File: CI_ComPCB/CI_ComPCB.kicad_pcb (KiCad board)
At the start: 2 copper layers, 145 x 101 mm, 30 parts, among them J1 Conn_01x15_Female, J10 Conn_01x02_Male, J1001 Conn_01x06_Female, J1002 Conn_01x06_Female, J1003 Conn_02x04_Odd_Even, J11 Conn_01x02_Male, J12 Conn_01x01_Female, J13 Conn_01x01_Female, J2 Conn_01x02_Male, J4 Conn_01x15_Female, J6 Conn_01x02_Male, J7 Conn_01x03_Male, J8 RJ45_LED_Shielded, J9 RJ45_LED_Shielded, Q1 IRF9540N, Q2 IRF9540N, U1 Boost_Converter, U1001 ESP32s

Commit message: Rough V1
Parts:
- removed Buck_Converter1: 12v_to_5V, RackCom:12vto5v
- removed Converter1, Converter2: TxRx-RS485, RackCom:TXRX-AB
- removed D1, D2, D3: 1N5400, Diode_THT:D_DO-201AD_P15.24mm_Horizontal
- removed HW-3731: Charger, RackCom:Charger
- removed Holder1: Battery-New_Library, RackCom:Battery
- removed J1, J4: Conn_01x15_Female, Connector_PinSocket_2.54mm:PinSocket_1x15_P2.54mm_Vertical
- removed J10, J11, J2, J6: Conn_01x02_Male, Connector_PinHeader_2.54mm:PinHeader_1x02_P2.54mm_Vertical
- removed J12, J13: Conn_01x01_Female, Connector_PinSocket_2.54mm:PinSocket_1x01_P2.54mm_Vertical
- removed J7: Conn_01x03_Male, Connector_PinHeader_2.54mm:PinHeader_1x03_P2.54mm_Vertical
- removed J8, J9: RJ45_LED_Shielded, Connector_RJ:RJ45_Amphenol_RJHSE538X
- removed Q1, Q2: IRF9540N, Package_TO_SOT_THT:TO-220-3_Vertical
- removed R1, R2, R3, R4: 330, Resistor_SMD:R_2512_6332Metric_Pad1.52x3.35mm_HandSolder
- removed U1: Boost_Converter, RackCom:BoostConverter
- added C1001: 4700pF, Capacitor_SMD:C_0805_2012Metric, F.Cu at (65.6, 100.5)
- added C1002: 0.1uF, Capacitor_SMD:C_0805_2012Metric, F.Cu at (69.0, 82.5)
- added C1003: 0.01uF, Capacitor_SMD:C_0805_2012Metric, F.Cu at (74.6, 94.4)
- added C1004: 4700pF, Capacitor_SMD:C_0805_2012Metric, F.Cu at (79.4, 90.9)
- added C1005: 33uF, Capacitor_SMD:C_0805_2012Metric, F.Cu at (97.4, 93.9)
- added C1006: 39pF, Capacitor_SMD:C_0805_2012Metric, F.Cu at (74.8, 89.0)
- added C1007: 33uF, Capacitor_SMD:C_0805_2012Metric, F.Cu at (97.2, 89.7)
- added Converter1001: TxRx-RS485, CI_ComPCB:TXRX-AB, F.Cu at (115.2, 122.1)
- added Converter1002: TxRx-RS485, CI_ComPCB:TXRX-AB, F.Cu at (115.0, 97.3)
- added D1001: 1N5400, Diode_THT:D_DO-201AD_P12.70mm_Horizontal, F.Cu at (96.6, 101.1)
- added D1002: B340A-13-F, digikey-footprints:DO-214AC, F.Cu at (87.1, 87.4)
- added D1003: 1N5400, Diode_THT:D_DO-201AD_P12.70mm_Horizontal, F.Cu at (110.7, 92.5)
- added J1004: Conn_01x15_Female, Connector_PinSocket_2.54mm:PinSocket_1x15_P2.54mm_Vertical, F.Cu at (104.7, 115.2)
- added J1005: Conn_01x06_Female, Connector_PinSocket_2.54mm:PinSocket_1x06_P2.54mm_Vertical, F.Cu at (110.8, 98.3)
- added J1006: Conn_01x06_Female, Connector_PinSocket_2.54mm:PinSocket_1x06_P2.54mm_Vertical, F.Cu at (111.6, 124.4)
- added J1007: Conn_01x02_Male, Connector_PinHeader_2.54mm:PinHeader_1x02_P2.54mm_Vertical, F.Cu at (104.0, 90.3)
- added J1008: Conn_01x02_Male, Connector_PinHeader_2.54mm:PinHeader_1x02_P2.54mm_Vertical, F.Cu at (69.2, 109.2)
- added J1009: RJ45_LED_Shielded, Connector_RJ:RJ45_Amphenol_RJHSE538X, F.Cu at (135.2, 86.8)
- added J1010: RJ45_LED_Shielded, Connector_RJ:RJ45_Amphenol_RJHSE538X, F.Cu at (142.0, 150.5)
- added J1011: Conn_01x01_Female, Connector_PinHeader_2.54mm:PinHeader_1x01_P2.54mm_Vertical, F.Cu at (122.9, 142.4)
- added J1012: Conn_01x01_Female, Connector_PinHeader_2.54mm:PinHeader_1x01_P2.54mm_Vertical, F.Cu at (151.8, 89.0)
- added J1013: Conn_02x04_Odd_Even, Connector_PinHeader_2.54mm:PinHeader_2x04_P2.54mm_Vertical, F.Cu at (132.7, 118.6)
- added L1001: 6.8uH, digikey-footprints:Inductor_13R106C, F.Cu at (97.0, 82.7)
- added Q1001: IRF9540N, digikey-footprints:TO-220-3, F.Cu at (76.8, 101.2)
- added R1001: 332k, Resistor_SMD:R_0805_2012Metric, F.Cu at (64.7, 95.3)
- added R1002: 68.1k, Resistor_SMD:R_0805_2012Metric, F.Cu at (68.8, 95.3)
- added R1003: 44.9K, Resistor_SMD:R_0805_2012Metric, F.Cu at (79.3, 86.9)
- added R1004: 10k, Resistor_SMD:R_0805_2012Metric, F.Cu at (103.6, 96.5)
- added R1005: 1.91k, Resistor_SMD:R_0805_2012Metric, F.Cu at (103.9, 102.0)
- added R1006: 330, Resistor_SMD:R_0805_2012Metric, F.Cu at (126.0, 85.6)
- added R1007: 330, Resistor_SMD:R_0805_2012Metric, F.Cu at (150.4, 157.2)
- added R1008: 330, Resistor_SMD:R_0805_2012Metric, F.Cu at (151.2, 82.9)
- added R1009: 330, Resistor_SMD:R_0805_2012Metric, F.Cu at (126.8, 142.3)
- added U1002: TPS54331, Package_SO:TI_SO-PowerPAD-8, F.Cu at (69.0, 89.0)
- J1001, J1002: value Conn_01x06_Female -> Conn_01x02_Male; footprint Connector_PinSocket_2.54mm:PinSocket_1x06_P2.54mm_Vertical -> Connector_PinHeader_2.54mm:PinHeader_1x02_P2.54mm_Vertical
- J1003: value Conn_02x04_Odd_Even -> Conn_01x15_Female; footprint Connector_PinHeader_2.00mm:PinHeader_2x04_P2.00mm_Vertical -> Connector_PinSocket_2.54mm:PinSocket_1x15_P2.54mm_Vertical
- U1001: footprint RackCom:ESP32s -> CI_ComPCB:ESP32s
- moved J1002 139.9 mm to (62.3, 150.7), turned to 180 degrees
- moved J1003 96.8 mm to (69.2, 115.3), turned to 0 degrees
- moved J1001 41.7 mm to (126.1, 90.2), turned to 0 degrees
- moved U1001 39.0 mm to (73.3, 107.6)
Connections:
- J1001 pad 1: Net-(J1001-Pad1) -> EPower
- J1001 pad 2: TX0 -> Net-(D1001-Pad1)
- J1002 pad 2: TX2 -> Vin
- U1001 pad D12: Net-(J1-Pad12) -> Net-(J1003-Pad12)
- U1001 pad D13: Net-(J1-Pad13) -> Net-(J1003-Pad13)
- U1001 pad D14: Net-(J1-Pad11) -> Net-(J1003-Pad11)
- U1001 pad D25: Net-(J1-Pad8) -> Net-(J1003-Pad8)
- U1001 pad D26: Net-(J1-Pad9) -> Net-(J1003-Pad9)
- U1001 pad D27: Net-(J1-Pad10) -> Net-(J1003-Pad10)
- U1001 pad D32: Net-(J1-Pad6) -> Net-(J1003-Pad6)
- U1001 pad D33: Net-(J1-Pad7) -> Net-(J1003-Pad7)
- U1001 pad D34: Net-(J1-Pad4) -> Net-(J1003-Pad4)
- U1001 pad D35: Net-(J1-Pad5) -> Net-(J1003-Pad5)
- U1001 pad EN: Net-(J1-Pad1) -> Net-(J1003-Pad1)
- U1001 pad VN: Net-(J1-Pad3) -> Net-(J1003-Pad3)
- U1001 pad VP: Net-(J1-Pad2) -> Net-(J1003-Pad2)
- U1001 pad Vin: Net-(J1-Pad15) -> Net-(J1002-Pad1)
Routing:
- net Sheild: track 268.6 -> 140.5 mm
- net Vin: track 131.8 -> 42.4 mm
- net Net-(J1003-Pad1): track 80.4 -> 5.37 mm
- net Net-(D1001-Pad1): track 0.00 -> 68.9 mm
- net Net-(J1003-Pad5): track 73.4 -> 5.37 mm
- net Net-(J1003-Pad3): track 72.1 -> 5.37 mm
- net Net-(J1003-Pad7): track 66.5 -> 5.37 mm
- net Net-(D1001-Pad2): track 0.00 -> 54.1 mm
- net Net-(HW-3731-Pad2): track 52.5 -> 0.00 mm
- net Net-(HW-3731-Pad6): track 51.1 -> 0.00 mm
- net Net-(J1010-Pad5): track 0.00 -> 50.5 mm
- net Net-(J1010-Pad4): track 0.00 -> 48.6 mm, vias 0 -> 1
- net GND: track 342.6 -> 296.6 mm, vias 0 -> 2
- net Net-(HW-3731-Pad3): track 44.8 -> 0.00 mm
- net Net-(J1010-Pad3): track 0.00 -> 44.4 mm
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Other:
- board size 145 x 101 mm -> 119.4 x 94 mm
- board text removed: "+"
- board text removed: "-"
- board text removed: "<-GND"
- board text removed: "}Battery"
- board text removed: "}Charging"

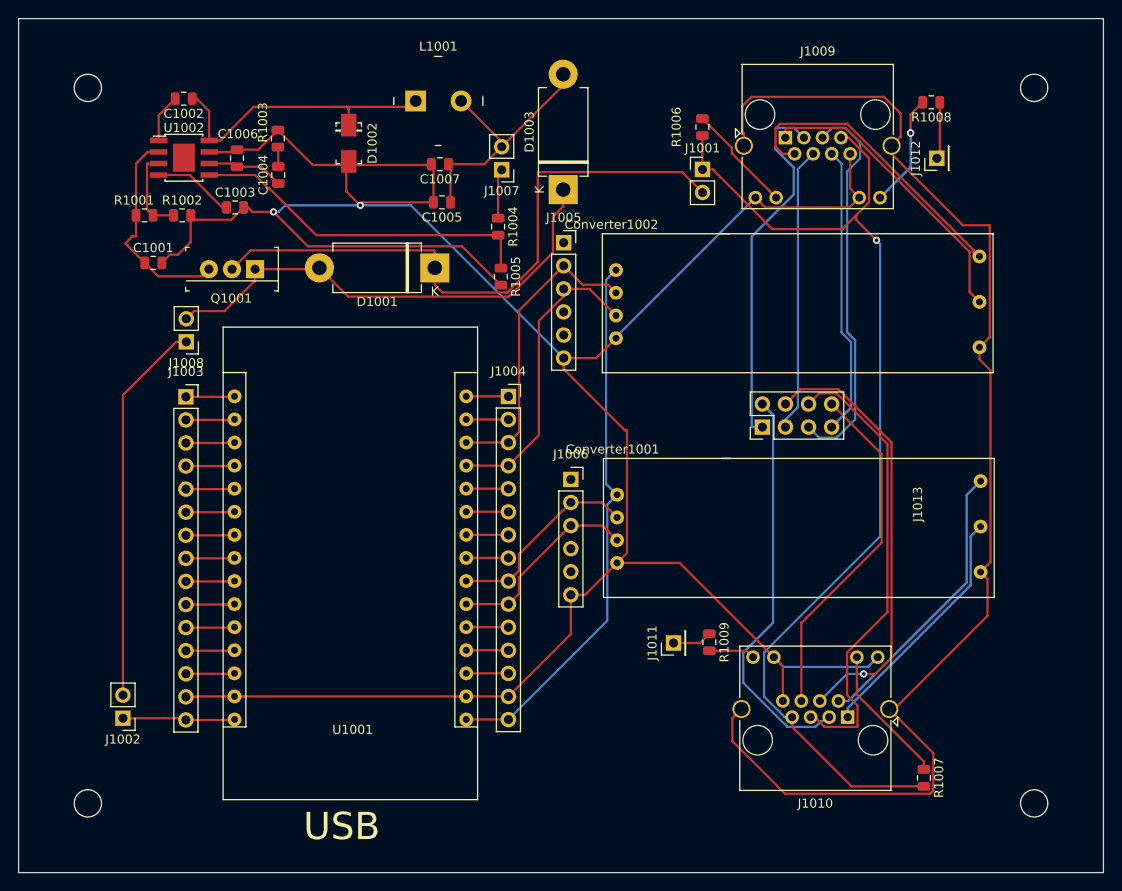
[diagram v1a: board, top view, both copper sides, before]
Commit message: V1 w/ no Battery
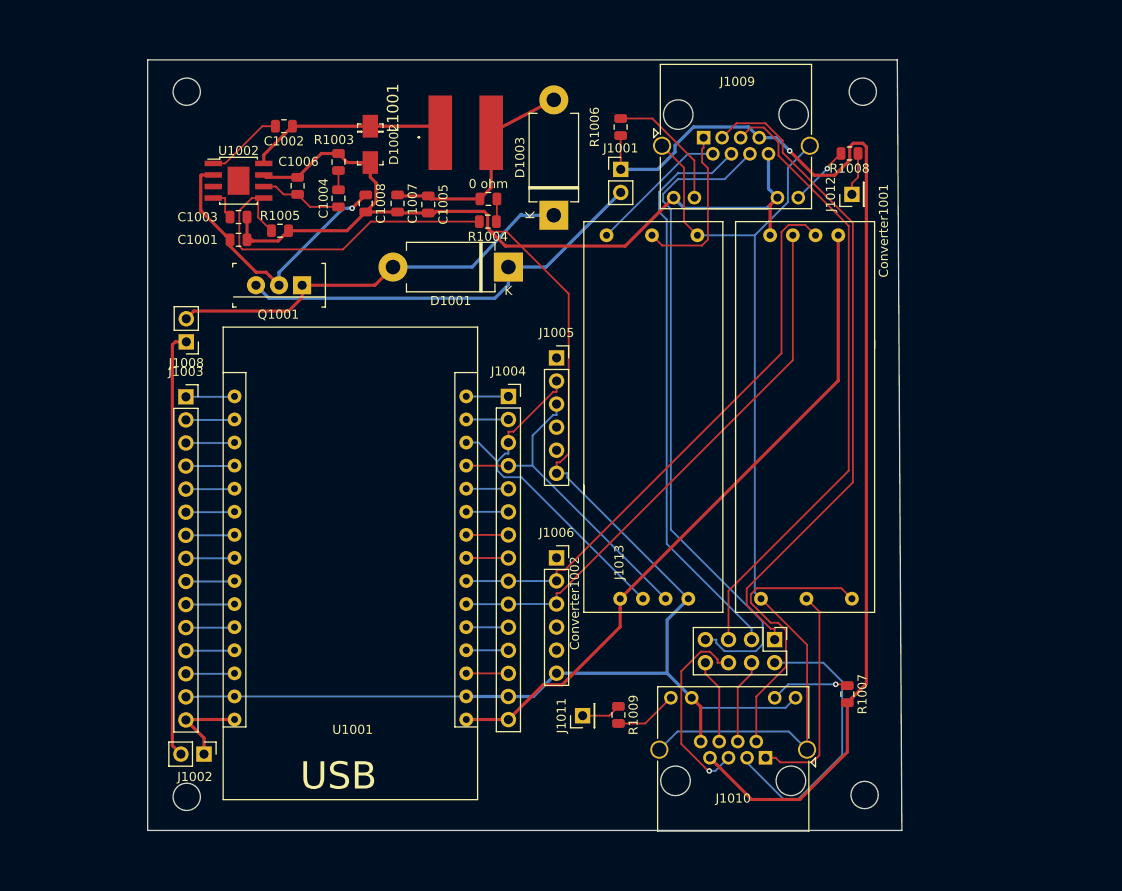
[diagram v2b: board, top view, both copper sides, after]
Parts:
- removed J1007: Conn_01x02_Male, Connector_PinHeader_2.54mm:PinHeader_1x02_P2.54mm_Vertical
- removed R1001: 332k, Resistor_SMD:R_0805_2012Metric
- removed R1002: 68.1k, Resistor_SMD:R_0805_2012Metric
- added 0 ohm: 0, Resistor_SMD:R_0805_2012Metric, F.Cu at (102.5, 93.5)
- added C1008: 10uF, Capacitor_SMD:C_0805_2012Metric, F.Cu at (89.0, 94.0)
- C1001: value 4700pF -> 10uF
- C1002: value 0.1uF -> 100nF
- C1003: value 0.01uF -> 8.2nF
- C1004: value 4700pF -> 1nF
- C1005, C1007: value 33uF -> 47uF
- C1006: value 39pF -> 10pf
- L1001: value 6.8uH -> SRN8040-100M; footprint digikey-footprints:Inductor_13R106C -> SamacSys_Parts:SRN8040100M
- R1003: value 44.9K -> 49.9k
- R1004: value 10k -> 10.2k
- moved Converter1002 41.7 mm to (113.0, 139.0), turned to 90 degrees
- moved Converter1001 39.6 mm to (145.0, 96.0), turned to 270 degrees
- moved R1005 24.8 mm to (79.6, 97.0), turned to 0 degrees
- moved J1013 23.4 mm to (134.0, 142.0), turned to 270 degrees
- moved J1011 12.8 mm to (112.9, 150.4)
- moved R1009 12.8 mm to (116.8, 150.3)
- moved J1005 12.7 mm to (110.0, 111.0)
- moved R1007 12.5 mm to (142.0, 148.0)
- moved C1002 11.4 mm to (80.0, 85.5)
- moved R1008 10.6 mm to (142.2, 88.5)
- moved J1012 10.2 mm to (142.5, 93.0)
- moved J1010 10.1 mm to (133.0, 155.0)
- moved J1002 9.76 mm to (71.2, 154.6), turned to 270 degrees
- moved C1001 9.72 mm to (75.0, 98.0)
- moved J1001 9.00 mm to (117.1, 90.2)
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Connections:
- Q1001 pad 2: Net-(D1001-Pad1) -> Net-(C1001-Pad1)
- Q1001 pad 3: Net-(C1001-Pad1) -> Net-(D1001-Pad1)
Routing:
- net GND: track 296.6 -> 250.4 mm, vias 2 -> 0
- net TX2: track 21.9 -> 63.7 mm
- net Net-(J1009-Pad6): track 31.8 -> 72.8 mm
- net RX2: track 21.9 -> 61.5 mm
- net Net-(J1010-Pad4): track 48.6 -> 9.31 mm, vias 1 -> 0
- net Sheild: track 140.5 -> 107.0 mm
- net Net-(J1009-Pad3): track 40.3 -> 72.6 mm
- net Net-(J1009-Pad4): track 31.3 -> 63.2 mm
- net Net-(J1010-Pad6): track 38.6 -> 9.31 mm
- net Net-(J1010-Pad5): track 50.5 -> 21.8 mm, vias 0 -> 1
- net Net-(J1009-Pad5): track 43.1 -> 68.7 mm
- net Net-(D1001-Pad1): track 68.9 -> 46.7 mm
- net A0: track 33.3 -> 15.4 mm
- net B0: track 32.9 -> 18.4 mm
- net 3.3V: track 60.0 -> 74.2 mm
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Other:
- board size 119.4 x 94 mm -> 83 x 84.8 mm
- net class Default: clearance 0.2 -> 0.254; trace_width 0.25 -> 0.2032; via_dia 0.8 -> 0.6096; via_drill 0.4 -> 0.4064
- net class power added: clearance 0.254, trace_width 0.3048, via_dia 0.889, via_drill 0.4064
- rule trace_clearance: 0.2 -> 0.254

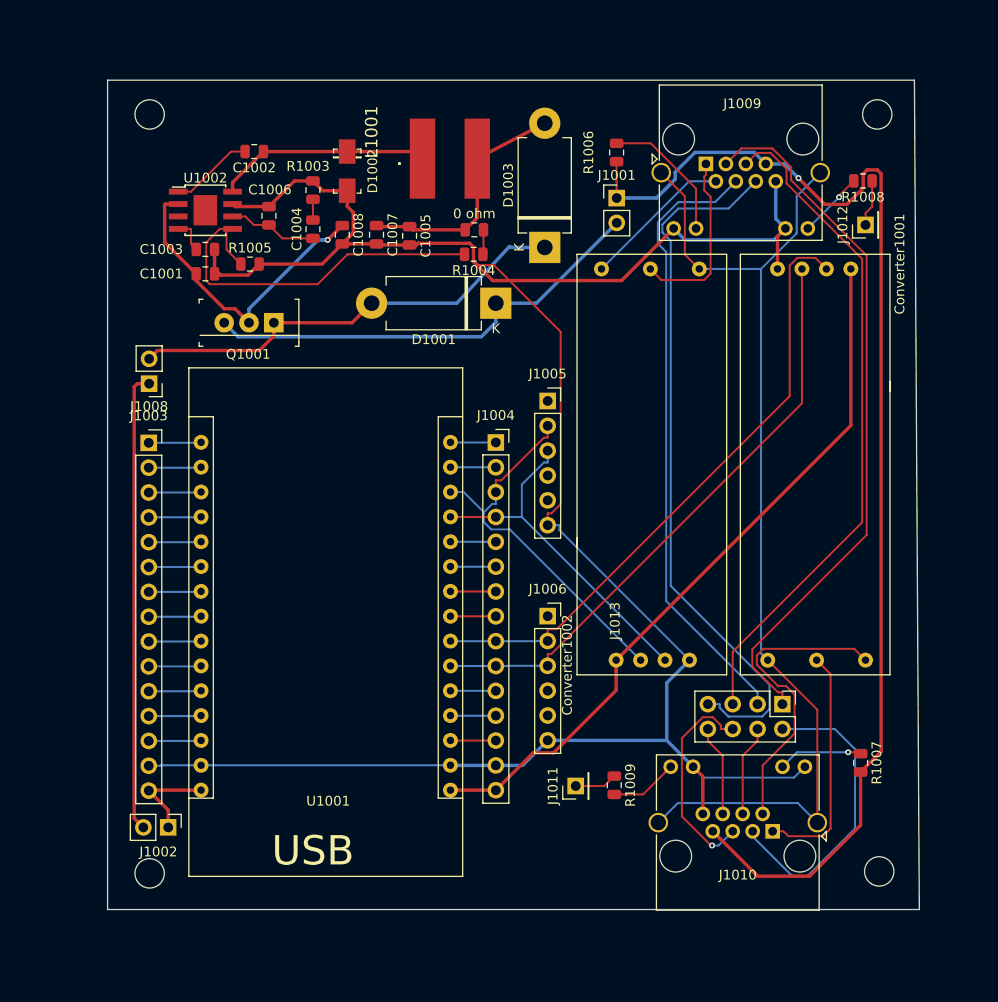
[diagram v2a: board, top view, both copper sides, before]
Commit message: V1 w/ no Battery
upgrade from first draft fixing issues #5 #20 #15  #12 #11 #6
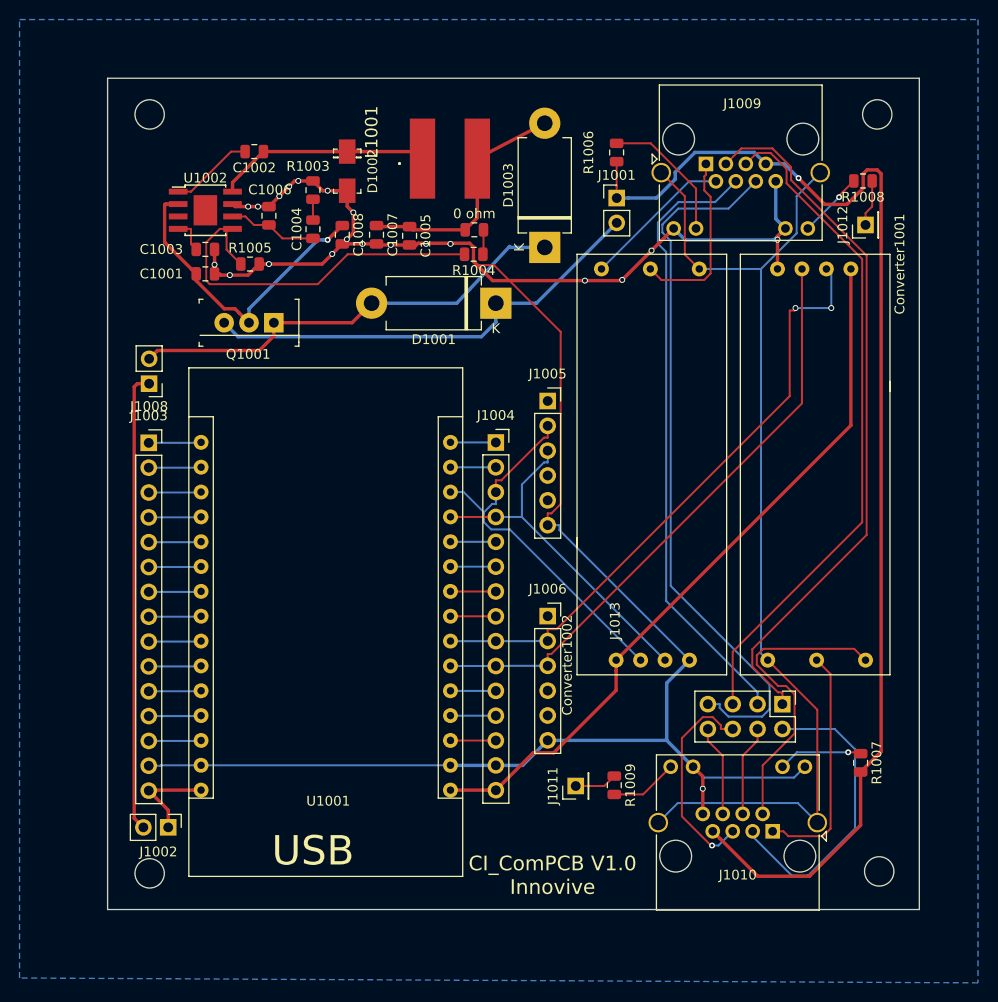
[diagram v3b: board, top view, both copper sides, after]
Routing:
- net TX2: track 63.7 -> 63.2 mm, vias 0 -> 2
- net GND: vias 0 -> 21
- added copper zone on B.Cu, net GND
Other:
- board size 83 x 84.8 mm -> 83 x 85 mm
- board text added: "CI_ComPCB V1.0 Innovive"
